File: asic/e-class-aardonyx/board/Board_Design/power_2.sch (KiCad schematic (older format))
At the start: 52 parts, among them Q1 FDN339AN, SW2 FSM2JSMAATR, U10 TPS7A7002DDAR, U11 ADM1186, U13 TPS7A7002DDAR, U14 74AUP1G09GW

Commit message: Updating footprint for test points
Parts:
- TP7, TP8, TP9: footprint Connector_PinHeader_2.54mm:PinHeader_1x01_P2.54mm_Vertical -> TestPoint:TestPoint_Pad_D1.5mm
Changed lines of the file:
@@
 F 0 "TP7" V 4053 6522 50  0000 C CNN
 F 1 "OUT3" V 4054 6522 50  0001 C CNN
-F 2 "Connector_PinHeader_2.54mm:PinHeader_1x01_P2.54mm_Vertical" H 4150 6450 50  0001 C CNN
+F 2 "TestPoint:TestPoint_Pad_D1.5mm" H 4150 6450 50  0001 C CNN
 F 3 "" H 4150 6450 50  0001 C CNN
 	1    3950 6450
@@
 F 0 "TP8" V 4053 6872 50  0000 C CNN
 F 1 "OUT4" V 4054 6872 50  0001 C CNN
-F 2 "Connector_PinHeader_2.54mm:PinHeader_1x01_P2.54mm_Vertical" H 4150 6800 50  0001 C CNN
+F 2 "TestPoint:TestPoint_Pad_D1.5mm" H 4150 6800 50  0001 C CNN
 F 3 "" H 4150 6800 50  0001 C CNN
 	1    3950 6800
@@
 F 0 "TP9" V 4053 7222 50  0000 C CNN
 F 1 "POWER_GOOD" V 4054 7222 50  0001 C CNN
-F 2 "Connector_PinHeader_2.54mm:PinHeader_1x01_P2.54mm_Vertical" H 4150 7150 50  0001 C CNN
+F 2 "TestPoint:TestPoint_Pad_D1.5mm" H 4150 7150 50  0001 C CNN
 F 3 "" H 4150 7150 50  0001 C CNN
 	1    3950 7150

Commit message: Updating placements
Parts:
- TP7, TP8, TP9: footprint TestPoint:TestPoint_Pad_D1.5mm -> TestPoint:TestPoint_Pad_D1.0mm
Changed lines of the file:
@@
 F 0 "TP7" V 4053 6522 50  0000 C CNN
 F 1 "OUT3" V 4054 6522 50  0001 C CNN
-F 2 "TestPoint:TestPoint_Pad_D1.5mm" H 4150 6450 50  0001 C CNN
+F 2 "TestPoint:TestPoint_Pad_D1.0mm" H 4150 6450 50  0001 C CNN
 F 3 "" H 4150 6450 50  0001 C CNN
 	1    3950 6450
@@
 F 0 "TP8" V 4053 6872 50  0000 C CNN
 F 1 "OUT4" V 4054 6872 50  0001 C CNN
-F 2 "TestPoint:TestPoint_Pad_D1.5mm" H 4150 6800 50  0001 C CNN
+F 2 "TestPoint:TestPoint_Pad_D1.0mm" H 4150 6800 50  0001 C CNN
 F 3 "" H 4150 6800 50  0001 C CNN
 	1    3950 6800
@@
 F 0 "TP9" V 4053 7222 50  0000 C CNN
 F 1 "POWER_GOOD" V 4054 7222 50  0001 C CNN
-F 2 "TestPoint:TestPoint_Pad_D1.5mm" H 4150 7150 50  0001 C CNN
+F 2 "TestPoint:TestPoint_Pad_D1.0mm" H 4150 7150 50  0001 C CNN
 F 3 "" H 4150 7150 50  0001 C CNN
 	1    3950 7150

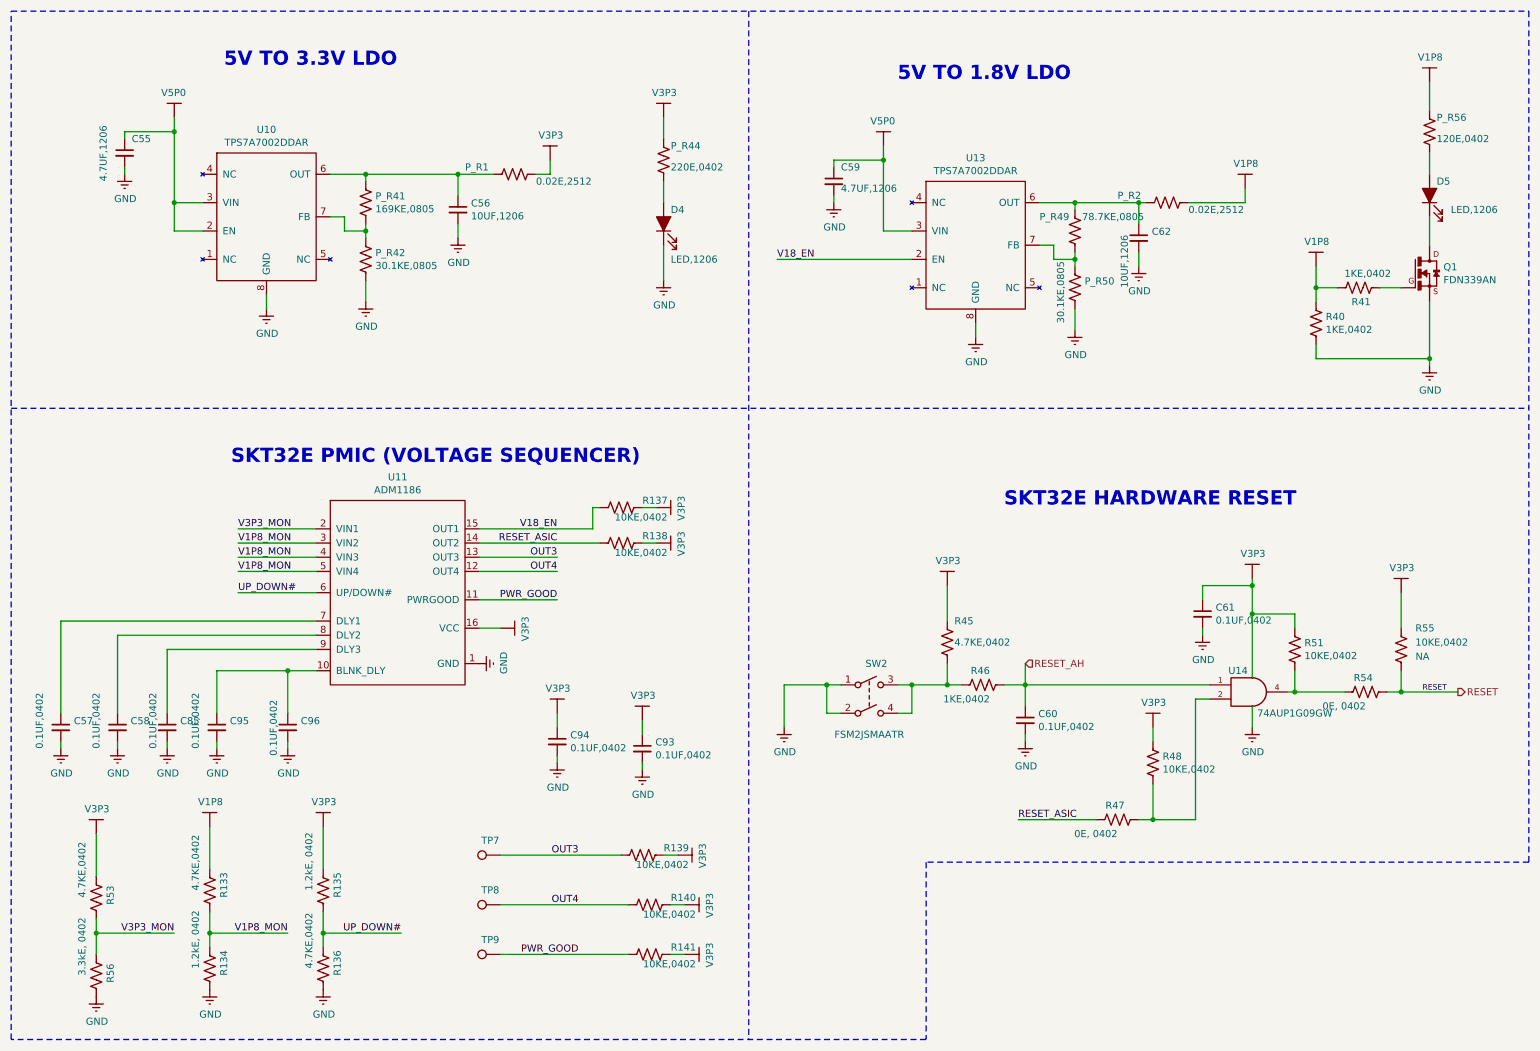
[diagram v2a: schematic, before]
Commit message: Updating 1x6 connector
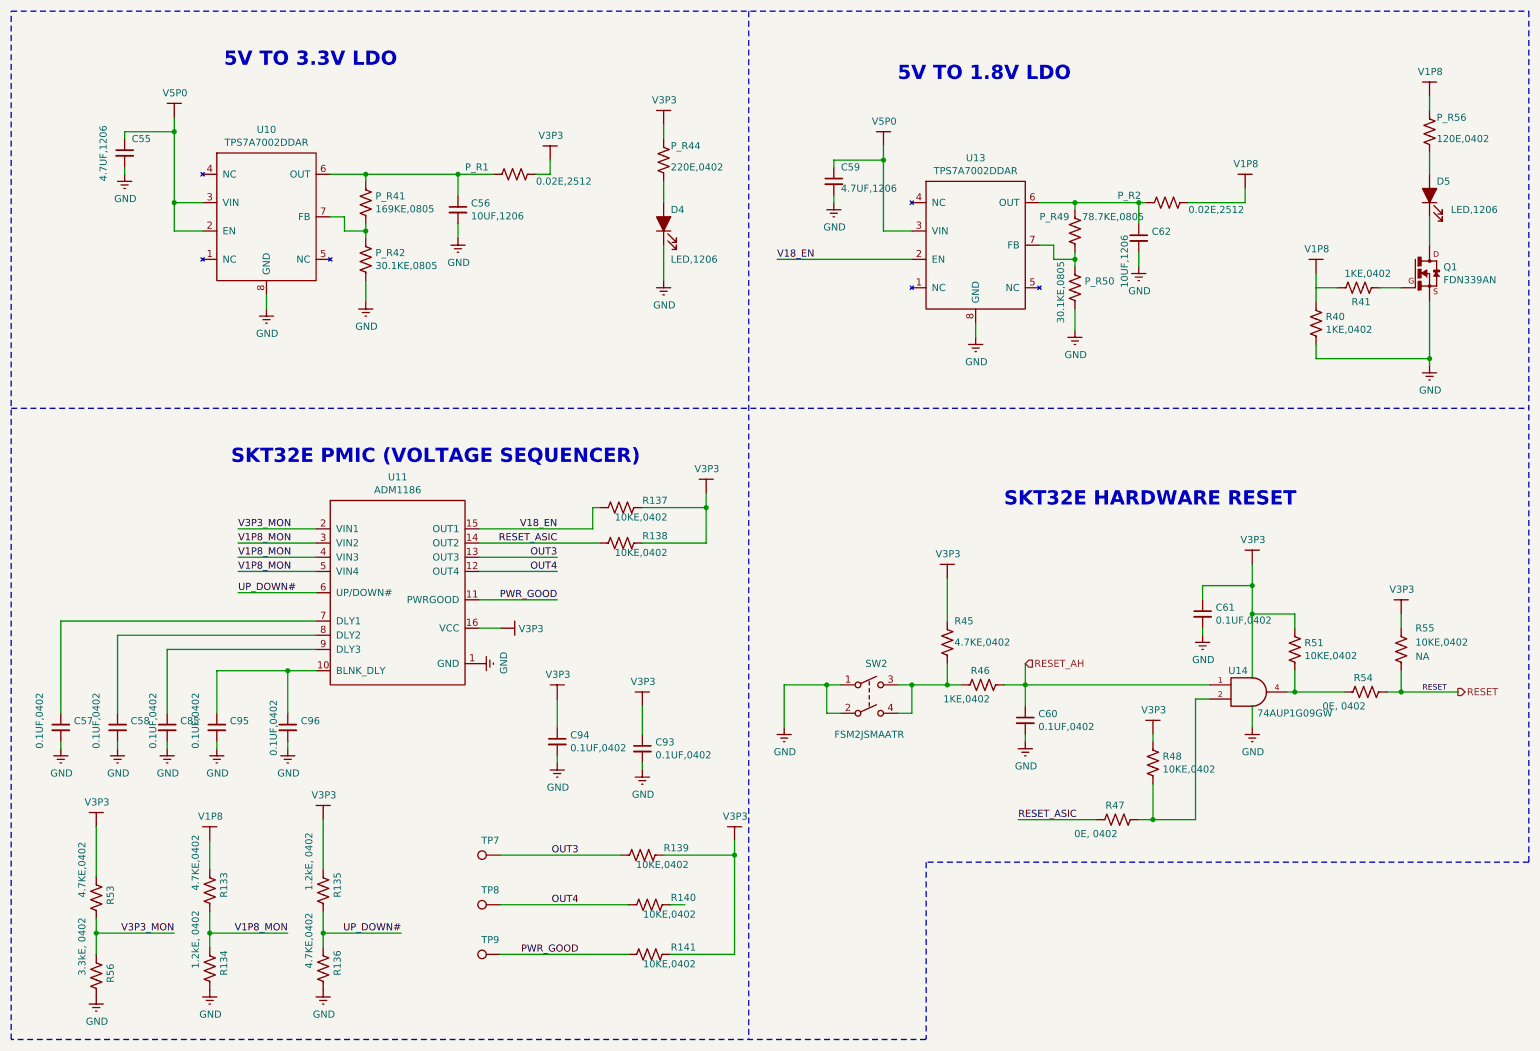
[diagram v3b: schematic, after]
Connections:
- net V3P3: no longer R140.1
